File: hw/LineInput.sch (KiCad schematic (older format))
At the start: 6 parts

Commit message: More work on PFC
Added more circuitry to PFC boost converter; about half done
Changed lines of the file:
@@
 Text Notes 4550 2100 0    50   ~ 0
 Common mode choke?\nPut in part and DNI?
+Text Label 7150 3250 0    50   ~ 0
+P
+Text Label 7150 3650 0    50   ~ 0
+N
+Text Label 3900 4300 0    50   ~ 0
+EARTH
 $EndSCHEMATC

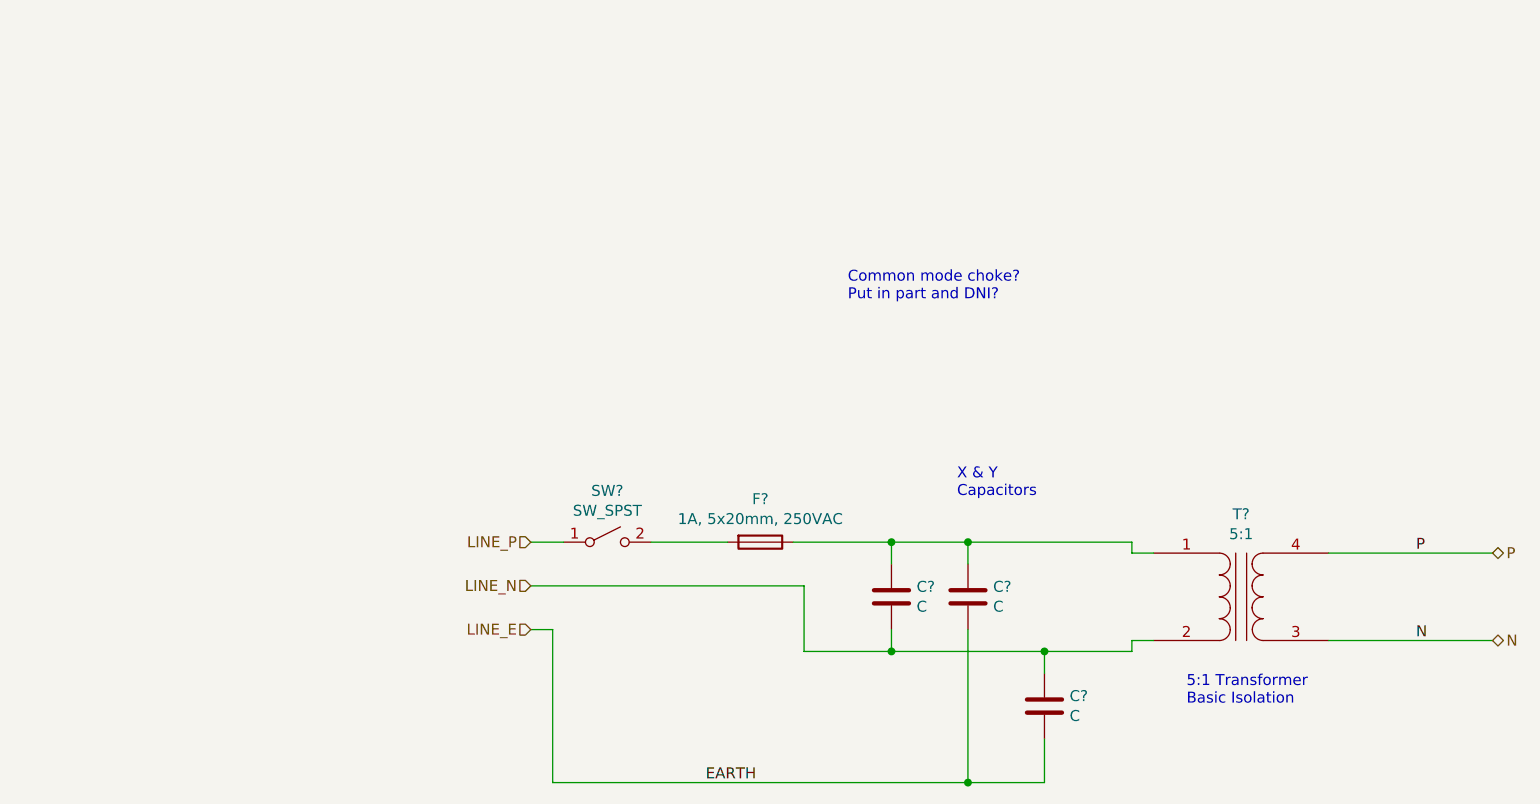
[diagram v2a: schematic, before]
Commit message: Cap selections
Lots of capacitor selections & datasheet downloads

Updated LTPowerCAD model with initial compensation values for primary switcher
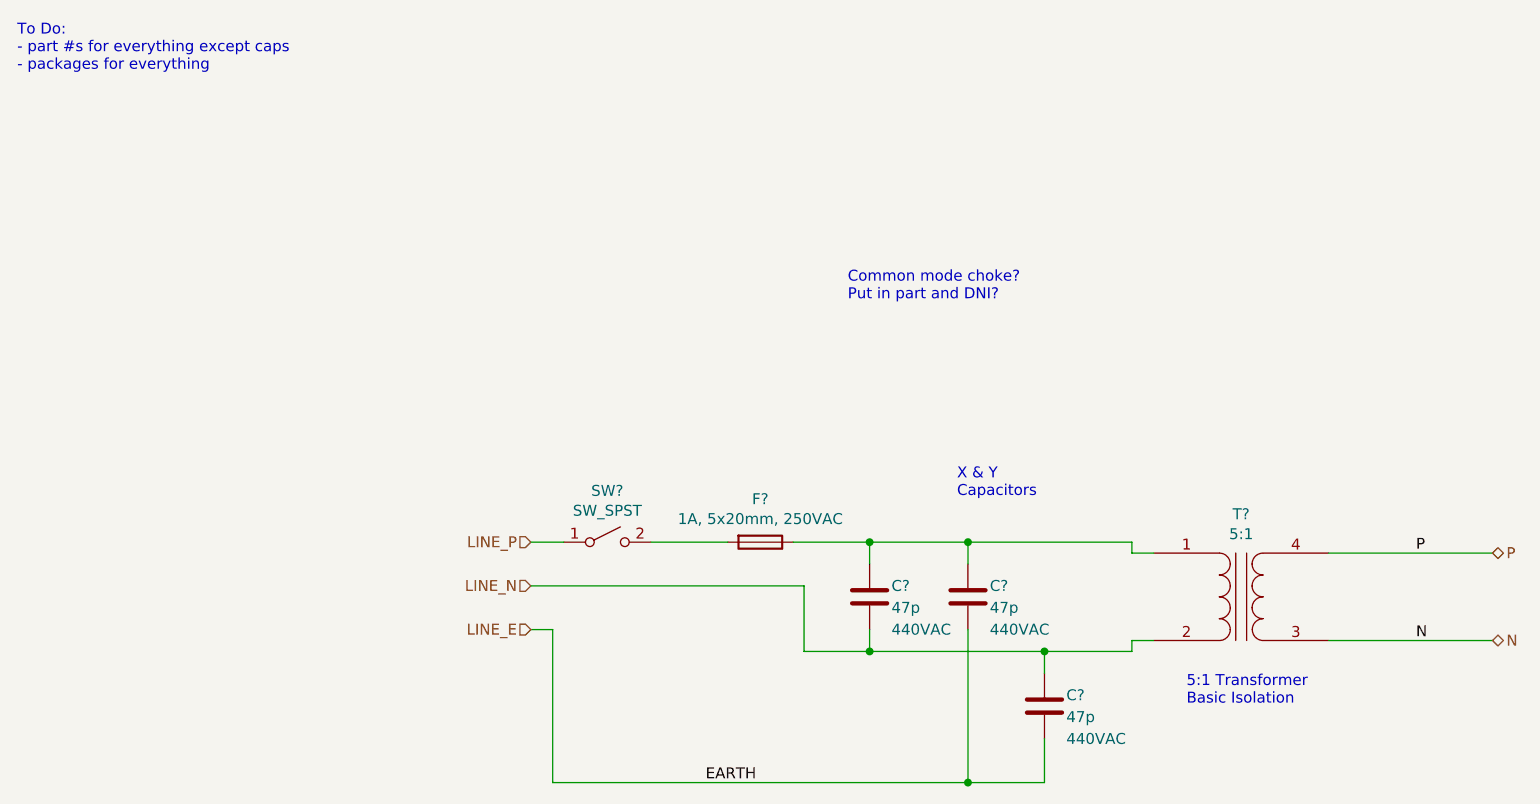
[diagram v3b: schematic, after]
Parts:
- removed C? (x2): C, symbol Device:C
- added C? (x2): 47p, symbol Device:C
- C?: value C -> 47p; MfrNum (none) -> Vishay_VY2470K29U2JS63V7; VRating (none) -> 440VAC
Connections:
- net LINE_E: now also C?.2, C?.2
- net LINE_N: now also C?.1
- net at C?.1, F?.1, T?.1 (AA): now also C?.1
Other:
- note added: "To Do:\n- part #s for everything except caps\n- packages for everything\n"
- moved on the sheet: C?
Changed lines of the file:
@@
 L Device:C C?
 U 1 1 5E80D59B
-P 4750 3450
-F 0 "C?" H 4865 3496 50  0000 L CNN
-F 1 "C" H 4865 3405 50  0000 L CNN
-F 2 "" H 4788 3300 50  0001 C CNN
-F 3 "~" H 4750 3450 50  0001 C CNN
-	1    4750 3450
-	1    0    0    -1
-$EndComp
-$Comp
-L Device:C C?
-U 1 1 5E80D606
-P 5100 3450
-F 0 "C?" H 5215 3496 50  0000 L CNN
-F 1 "C" H 5215 3405 50  0000 L CNN
-F 2 "" H 5138 3300 50  0001 C CNN
-F 3 "~" H 5100 3450 50  0001 C CNN
-	1    5100 3450
-	1    0    0    -1
-$EndComp
-$Comp
-L Device:C C?
-U 1 1 5E80D628
-P 5450 3950
-F 0 "C?" H 5565 3996 50  0000 L CNN
-F 1 "C" H 5565 3905 50  0000 L CNN
-F 2 "" H 5488 3800 50  0001 C CNN
-F 3 "~" H 5450 3950 50  0001 C CNN
-	1    5450 3950
+P 4650 3450
+F 0 "C?" H 4750 3500 50  0000 L CNN
+F 1 "47p" H 4750 3400 50  0000 L CNN
+F 2 "" H 4688 3300 50  0001 C CNN
+F 3 "~" H 4650 3450 50  0001 C CNN
+F 4 "Vishay_VY2470K29U2JS63V7" H 4650 3450 50  0001 C CNN "MfrNum"
+F 5 "440VAC" H 4750 3300 50  0000 L CNN "VRating"
+	1    4650 3450
 	1    0    0    -1
 $EndComp
 Wire Wire Line
-	4300 3200 4750 3200
+	4300 3200 4650 3200
 Wire Wire Line
 	5100 3200 5100 3300
 Wire Wire Line
-	4750 3300 4750 3200
-Connection ~ 4750 3200
+	4650 3300 4650 3200
+Connection ~ 4650 3200
 Wire Wire Line
-	4750 3200 5100 3200
+	4650 3200 5100 3200
 Wire Wire Line
 	4350 3400 4350 3700
 Wire Wire Line
-	4350 3700 4750 3700
+	4350 3700 4650 3700
 Wire Wire Line
-	4750 3600 4750 3700
-Connection ~ 4750 3700
+	4650 3600 4650 3700
+Connection ~ 4650 3700
 Wire Wire Line
-	4750 3700 5450 3700
+	4650 3700 5450 3700
 Wire Wire Line
 	3200 3600 3100 3600
@@
 Text Label 3900 4300 0    50   ~ 0
 EARTH
+$Comp
+L Device:C C?
+U 1 1 5EC17EEF
+P 5100 3450
+F 0 "C?" H 5200 3500 50  0000 L CNN
+F 1 "47p" H 5200 3400 50  0000 L CNN
+F 2 "" H 5138 3300 50  0001 C CNN
+F 3 "~" H 5100 3450 50  0001 C CNN
+F 4 "Vishay_VY2470K29U2JS63V7" H 5100 3450 50  0001 C CNN "MfrNum"
+F 5 "440VAC" H 5200 3300 50  0000 L CNN "VRating"
+	1    5100 3450
+	1    0    0    -1
+$EndComp
+$Comp
+L Device:C C?
+U 1 1 5EC17F17
+P 5450 3950
+F 0 "C?" H 5550 4000 50  0000 L CNN
+F 1 "47p" H 5550 3900 50  0000 L CNN
+F 2 "" H 5488 3800 50  0001 C CNN
+F 3 "~" H 5450 3950 50  0001 C CNN
+F 4 "Vishay_VY2470K29U2JS63V7" H 5450 3950 50  0001 C CNN "MfrNum"
+F 5 "440VAC" H 5550 3800 50  0000 L CNN "VRating"
+	1    5450 3950
+	1    0    0    -1
+$EndComp
+Text Notes 750  1050 0    50   ~ 0
+To Do:\n- part #s for everything except caps\n- packages for everything\n
 $EndSCHEMATC

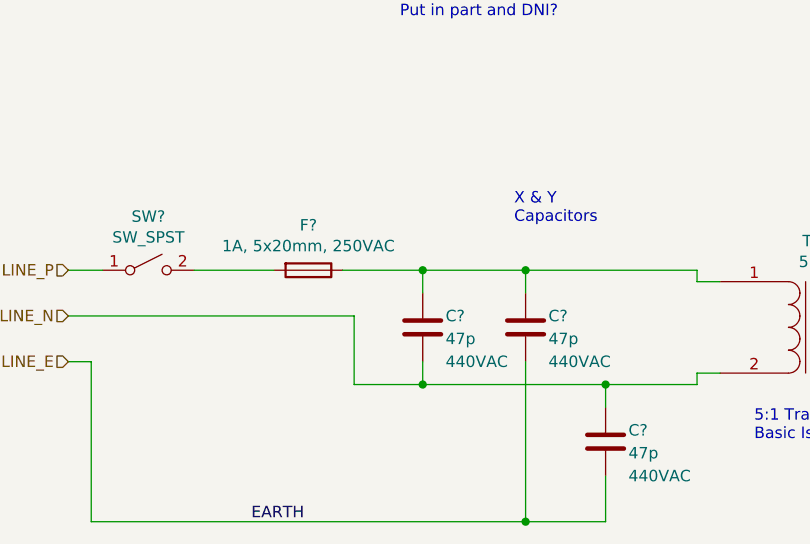
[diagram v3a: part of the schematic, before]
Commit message: more component selection
more caps selected; updated primary switcher sim file
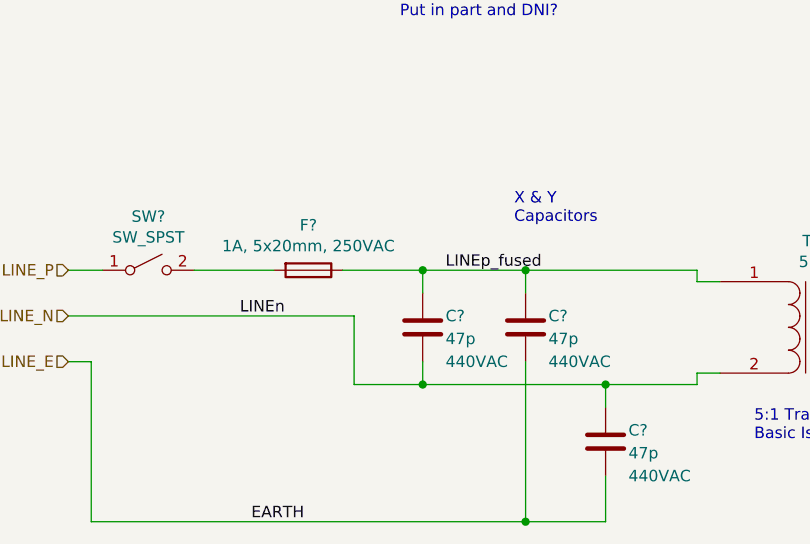
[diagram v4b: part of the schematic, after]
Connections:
- net LINEp_fused: now reaches C?.1, C?.1, F?.1, T?.1 (AA)
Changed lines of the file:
@@
 Text Notes 750  1050 0    50   ~ 0
 To Do:\n- part #s for everything except caps\n- packages for everything\n
+Text Label 4750 3200 0    50   ~ 0
+LINEp_fused
+Text Label 3850 3400 0    50   ~ 0
+LINEn
 $EndSCHEMATC
